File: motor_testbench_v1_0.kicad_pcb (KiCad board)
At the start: 4 copper layers, 130.5 x 74 mm, 156 parts, among them J1 Conn_01x03_Pin, J10 Conn_01x02_Pin, J11 Conn_01x02_Pin, J2 Conn_01x18_Pin, J3 V_bat_in, J4 V_bat_out, J5 Conn_01x05_Pin, J6 Conn_01x05_Pin, J7 Conn_01x05_Pin, J8 Conn_01x02_Pin, J9 V_bat_secondary, U1 ESP32-S3-DevKitC, U10 TPS7A20xxxDQN, U11 MCP1501-18xSN, U3 MCP6022, U4 ACPL-C87A, U5 TPS62933, U6 TLV77333PDBVR, U7 TPS62933, U8 TLV77333PDBVR, U9 TPS7A20xxxDQN

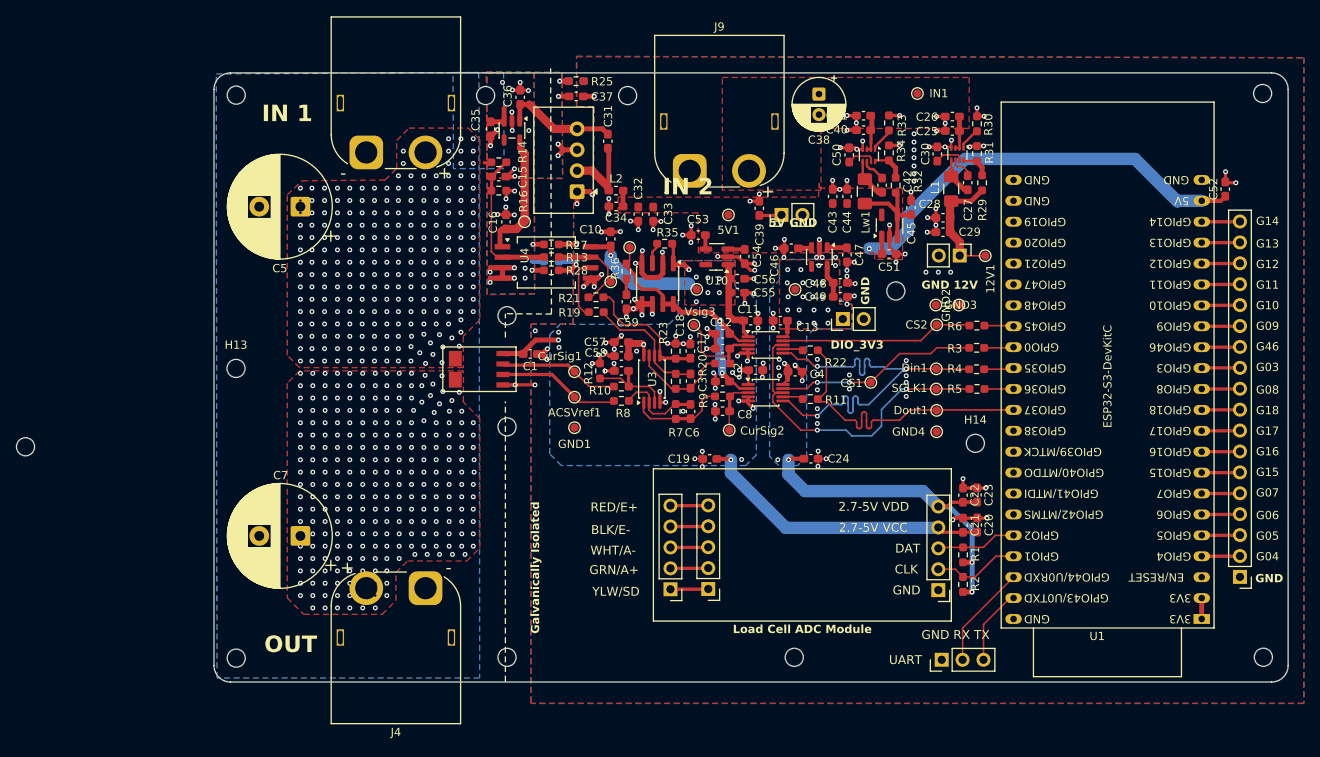
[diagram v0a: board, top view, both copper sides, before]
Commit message: Improved layout, added TVS diodes. Rotated ESP32, Changed proper SPI pins, finalized the load cell module area.
[KiCad Version: 9.0.8]
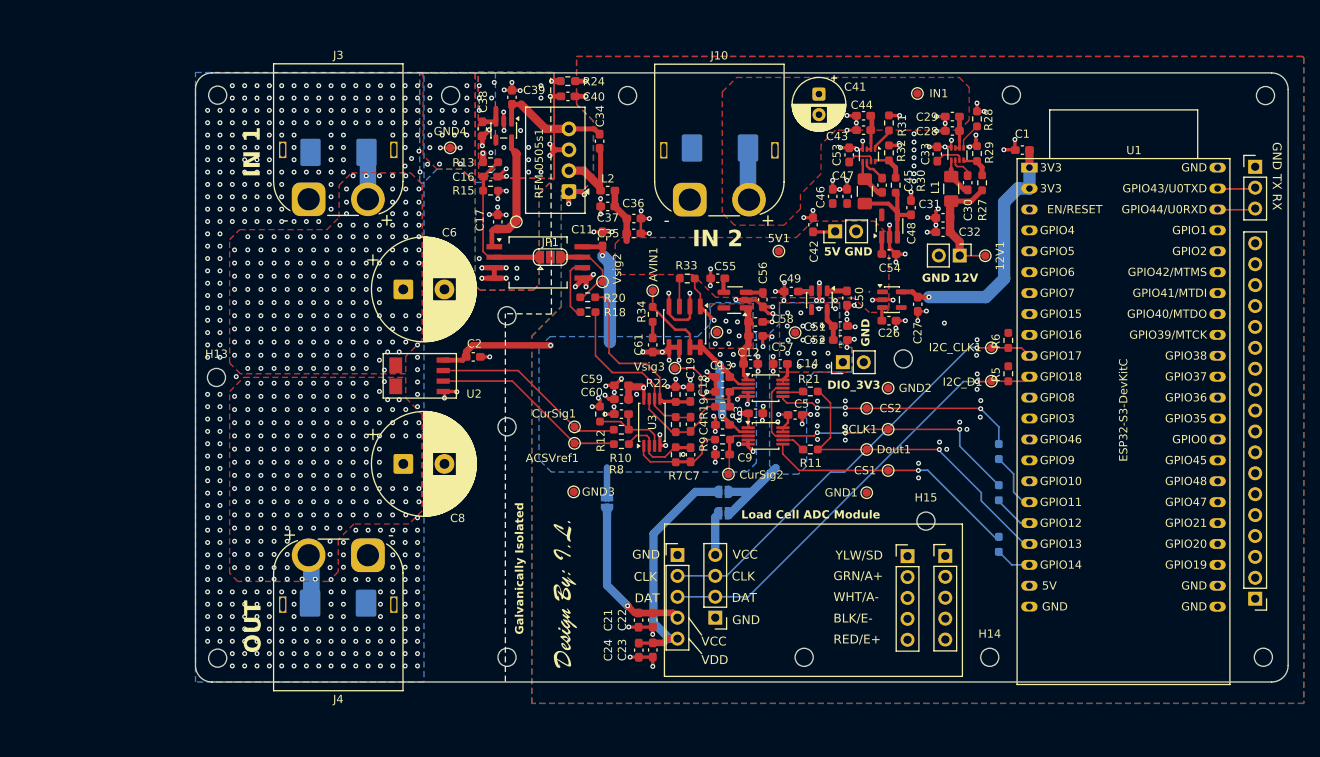
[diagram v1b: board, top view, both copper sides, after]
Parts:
- removed the C19 at (133.7, 86.4)
- removed the C24 at (146.0, 86.4)
- removed the C52 at (196.4, 53.6)
- removed Din1: TestPoint, TestPoint:TestPoint_Pad_D1.0mm
- removed the R13 at (114.5, 61.9)
- removed R26: 0R, Resistor_SMD:R_0603_1608Metric_Pad0.98x0.95mm_HandSolder
- removed the R27 at (114.5, 60.3)
- removed the R28 at (114.5, 63.5)
- removed the R4 at (166.2, 75.5)
- added C1: 1u, Capacitor_SMD:C_0603_1608Metric_Pad1.08x0.95mm_HandSolder, F.Cu at (171.7, 48.9)
- added C26: 1u, Capacitor_SMD:C_0603_1608Metric_Pad1.08x0.95mm_HandSolder, F.Cu at (155.5, 69.6)
- added C27: 2.2u, Capacitor_SMD:C_0603_1608Metric_Pad1.08x0.95mm_HandSolder, F.Cu at (159.0, 67.6)
- added D1: 1.5SMCxxCA, Diode_SMD:D_SMC, B.Cu at (88.6, 49.1)
- added D2: 1.5SMCxxCA, Diode_SMD:D_SMC, B.Cu at (88.6, 103.9)
- added D3: 1.5SMCxxCA, Diode_SMD:D_SMC, B.Cu at (135.0, 48.6)
- added G***: LOGO, LOGO, F.Cu at (117.8, 100.5)
- added G***: LOGO, LOGO, B.Cu at (181.5, 111.3)
- added H15: MountingHole, MountingHole:MountingHole_2.2mm_M2_DIN965, F.Cu at (160.0, 94.0)
- added I2C_CLK1: TestPoint, TestPoint:TestPoint_Pad_D1.0mm, F.Cu at (167.9, 72.9)
- added I2C_D1: TestPoint, TestPoint:TestPoint_Pad_D1.0mm, F.Cu at (167.9, 77.0)
- added J8: Conn_01x04_Pin, Connector_PinHeader_2.54mm:PinHeader_1x04_P2.54mm_Vertical, F.Cu at (134.4, 105.7)
- added JP1: SolderJumper_3_Open, Jumper:SolderJumper-3_P1.3mm_Open_RoundedPad1.0x1.5mm, F.Cu at (114.3, 61.9)
- added JP2: SolderJumper_2_Open, Jumper:SolderJumper-2_P1.3mm_Open_RoundedPad1.0x1.5mm, B.Cu at (121.2, 91.7)
- added JP3: SolderJumper_2_Open, Jumper:SolderJumper-2_P1.3mm_Open_RoundedPad1.0x1.5mm, B.Cu at (135.4, 90.4)
- added JP4: SolderJumper_2_Open, Jumper:SolderJumper-2_P1.3mm_Open_RoundedPad1.0x1.5mm, B.Cu at (135.4, 93.0)
- added JP5: SolderJumper_3_Open, Jumper:SolderJumper-3_P1.3mm_Open_RoundedPad1.0x1.5mm, B.Cu at (114.3, 61.9)
- added U5: TLV77333PDBVR, Package_TO_SOT_SMD:SOT-23-5, F.Cu at (155.9, 67.0)
- J10: renamed from J9; footprint Connector_AMASS:AMASS_XT60PW-M_1x02_P7.20mm_Horizontal -> custom_footprints:AMASS_XT60PW-M_1x02_P7.20mm_Horizontal_with3DModel
- J3, J4: footprint Connector_AMASS:AMASS_XT60PW-M_1x02_P7.20mm_Horizontal -> custom_footprints:AMASS_XT60PW-M_1x02_P7.20mm_Horizontal_with3DModel
- R2: renamed from R6; moved to B.Cu
- R3: renamed from R5; moved to B.Cu
- R4: renamed from R3; moved to B.Cu
- RFM-0505s1: footprint Converter_DCDC:Converter_DCDC_TRACO_TBA1-xxxx_THT -> custom_footprints:Converter_DCDC_TRACO_TBA1-xxxx_THT_with_3DModel
- U1: footprint ESP_footprints:ESP32-S3-DevKitC -> custom_footprints:ESP32-S3-DevKitC_with_3DModel
- U2: footprint custom_footprints:SOIC-6 -> custom_footprints:ACS37030LLZATR-065B3
- moved H3 107.2 mm to (157.2, 74.2)
- moved H1 73.2 mm to (170.4, 42.2)
- moved J1 71.0 mm to (200.0, 50.9), turned to 0 degrees
- moved GND4 68.4 mm to (102.2, 48.6)
- moved U1 58.7 mm to (172.6, 51.0), turned to 0 degrees
- moved GND3 49.5 mm to (117.2, 90.4)
- moved H2 45.9 mm to (145.2, 110.5)
- moved C24 45.2 mm to (125.1, 109.6), turned to 90 degrees
- moved C21 42.7 mm to (125.1, 106.0), turned to 90 degrees
- moved C23 42.1 mm to (126.8, 109.6), turned to 90 degrees
- moved C22 39.4 mm to (126.8, 106.0), turned to 90 degrees
- moved GND1 36.4 mm to (152.8, 90.5)
- moved J6 33.6 mm to (162.3, 98.2), turned to 0 degrees
- moved J7 32.0 mm to (129.8, 98.1), turned to 0 degrees
- moved R6 30.2 mm to (170.0, 72.0), turned to -90 degrees
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- renumbered C9 to C10, C10 to C11, C11 to C12, C12 to C13, C13 to C14, C14 to C15, C15 to C16, C16 to C17, C17 to C18, C18 to C19, C1 to C2, C20 to C21, C21 to C22, C22 to C23, C23 to C24, C25 to C28, C26 to C29, C2 to C3, C27 to C30, C28 to C31, C29 to C32, C30 to C33, C31 to C34, C32 to C35, C33 to C36, C34 to C37, C35 to C38, C36 to C39, C3 to C4, C37 to C40, C38 to C41, C39 to C42, C40 to C43, C41 to C44, C42 to C45, C43 to C46, C44 to C47, C45 to C48, C46 to C49, C4 to C5, C47 to C50, C48 to C51, C49 to C52, C50 to C53, C51 to C54, C53 to C55, C54 to C56, C55 to C57, C56 to C58, C57 to C59, C5 to C6, C58 to C60, C59 to C61, C6 to C7, C7 to C8, C8 to C9, J10 to J11, J11 to J12, J8 to J9, R14 to R13, R16 to R15, R18 to R17, R19 to R18, R20 to R19, R21 to R20, R22 to R21, R23 to R22, R24 to R23, R25 to R24, R29 to R27, R30 to R28, R31 to R29, R32 to R30, R33 to R31, R34 to R32, R35 to R33, R36 to R34, R1 to R5, R2 to R6, U9 to U10, U10 to U11, U11 to U12, U5 to U6, U6 to U7, U7 to U8, U8 to U9
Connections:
- C21 pad 2: 3V3_ANA -> Net-(J7-Pin_4)
- C22 pad 2: 3V3_ANA -> Net-(J7-Pin_4)
- C23 pad 2: 3V3_DIO -> Net-(J7-Pin_5)
- C24 pad 2: 3V3_DIO -> Net-(J7-Pin_5)
- Dout1 pad 1: D_out -> MISO
- GND4 pad 1: GND -> GND_ISO
- J5 pad 1: Net-(J5-Pin_1) -> unconnected-(J5-Pin_1-Pad1)
- J5 pad 2: Net-(J5-Pin_2) -> unconnected-(J5-Pin_2-Pad2)
- J5 pad 3: Net-(J5-Pin_3) -> unconnected-(J5-Pin_3-Pad3)
- J5 pad 4: Net-(J5-Pin_4) -> unconnected-(J5-Pin_4-Pad4)
- J5 pad 5: Net-(J5-Pin_5) -> unconnected-(J5-Pin_5-Pad5)
- J6 pad 1: Net-(J5-Pin_1) -> unconnected-(J6-Pin_1-Pad1)
- J6 pad 2: Net-(J5-Pin_2) -> unconnected-(J6-Pin_2-Pad2)
- J6 pad 3: Net-(J5-Pin_3) -> unconnected-(J6-Pin_3-Pad3)
- J6 pad 4: Net-(J5-Pin_4) -> unconnected-(J6-Pin_4-Pad4)
- J6 pad 5: Net-(J5-Pin_5) -> unconnected-(J6-Pin_5-Pad5)
- J7 pad 4: 3V3_ANA -> Net-(J7-Pin_4)
- J7 pad 5: 3V3_DIO -> Net-(J7-Pin_5)
- MCP1 pad 6: D_in -> CS1
- MCP1 pad 9: CS1 -> 3V3_DIO
- MCP2 pad 6: D_in -> CS2
- MCP2 pad 9: CS2 -> 3V3_DIO
- R11 pad 2: D_out -> MISO
- R2 pad 1: Net-(U1-GPIO45) -> Net-(U1-GPIO11/ADC2_CH0)
- R21 pad 2: D_out -> MISO
- R3 pad 1: Net-(U1-GPIO36) -> Net-(U1-GPIO12/ADC2_CH1)
- R4 pad 1: Net-(U1-GPIO0) -> Net-(U1-GPIO14/ADC2_CH3)
- R5 pad 1: 3V3_DIO -> ESP_3V3
- R6 pad 1: 3V3_DIO -> ESP_3V3
- U1 pad 1: Net-(U1-3V3-Pad1) -> ESP_3V3
- U1 pad 10: /10 -> I2C_CLK
- U1 pad 11: /11 -> I2C_D
- U1 pad 12: /12 -> unconnected-(U1-GPIO8/ADC1_CH7-Pad12)
- U1 pad 13: /13 -> unconnected-(U1-GPIO3/ADC1_CH2-Pad13)
- U1 pad 14: /46 -> unconnected-(U1-GPIO46-Pad14)
- U1 pad 15: /15 -> unconnected-(U1-GPIO9/ADC1_CH8-Pad15)
- U1 pad 16: /16 -> unconnected-(U1-GPIO10/ADC1_CH9-Pad16)
- U1 pad 17: /17 -> Net-(U1-GPIO11/ADC2_CH0)
- U1 pad 18: /18 -> Net-(U1-GPIO12/ADC2_CH1)
- U1 pad 19: /19 -> MISO
- U1 pad 2: Net-(U1-3V3-Pad1) -> ESP_3V3
- U1 pad 20: /20 -> Net-(U1-GPIO14/ADC2_CH3)
- U1 pad 21: 5V_bus -> unconnected-(U1-5V-Pad21)
- U1 pad 30: Net-(U1-GPIO45) -> unconnected-(U1-GPIO45-Pad30)
- U1 pad 31: Net-(U1-GPIO0) -> unconnected-(U1-GPIO0-Pad31)
- U1 pad 32: Net-(U1-GPIO35) -> unconnected-(U1-GPIO35-Pad32)
- U1 pad 33: Net-(U1-GPIO36) -> unconnected-(U1-GPIO36-Pad33)
- U1 pad 34: D_out -> unconnected-(U1-GPIO37-Pad34)
- U1 pad 4: /4 -> unconnected-(U1-GPIO4/ADC1_CH3-Pad4)
- U1 pad 40: I2C_D -> unconnected-(U1-GPIO2/ADC1_CH1-Pad40)
- U1 pad 41: I2C_CLK -> unconnected-(U1-GPIO1/ADC1_CH0-Pad41)
- U1 pad 42: Net-(J1-Pin_2) -> Net-(J1-Pin_3)
- U1 pad 43: Net-(J1-Pin_3) -> Net-(J1-Pin_2)
- U1 pad 5: /5 -> unconnected-(U1-GPIO5/ADC1_CH4-Pad5)
- U1 pad 6: /6 -> unconnected-(U1-GPIO6/ADC1_CH5-Pad6)
- U1 pad 7: /7 -> unconnected-(U1-GPIO7/ADC1_CH6-Pad7)
- U1 pad 8: /8 -> unconnected-(U1-GPIO15/ADC2_CH4/32K_P-Pad8)
- U1 pad 9: /9 -> unconnected-(U1-GPIO16/ADC2_CH5/32K_N-Pad9)
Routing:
- net D_in: track 51.7 -> 0.00 mm, vias 3 -> 0
- net 5V_bus: track 65.4 -> 20.5 mm, vias 1 -> 0
- net I2C_D: track 9.59 -> 53.9 mm, vias 0 -> 1
- net I2C_CLK: track 10.6 -> 54.9 mm, vias 0 -> 1
- net MISO: track 0.00 -> 39.5 mm, vias 0 -> 1
- net D_out: track 37.5 -> 0.00 mm
- net ESP_3V3: track 0.00 -> 31.8 mm, vias 0 -> 1
- net 3V3_DIO: track 53.3 -> 22.0 mm, vias 23 -> 20
- net Net-(J7-Pin_5): track 0.00 -> 29.4 mm
- net 3V3_ANA: track 82.5 -> 56.8 mm, vias 12 -> 11
- net Net-(J7-Pin_4): track 0.00 -> 20.5 mm, vias 0 -> 1
- net /Measurements/V_bat_in: track 1.03 -> 17.6 mm, vias 238 -> 174
- net GND: track 171.3 -> 160.3 mm, vias 159 -> 156
- net /Measurements/ACS_VREF: track 15.0 -> 24.3 mm
- net /Measurements/cur_sig: track 14.6 -> 23.8 mm
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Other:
- board size 130.5 x 74 mm -> 132.8 x 74 mm
- board text added: "GND TX RX"
- board text added: "VCC"
- board text added: "VDD"
- board text removed: "2.7-5V VCC"
- board text removed: "2.7-5V VDD"
- board text removed: "G03"
- board text removed: "G04"
- board text removed: "G05"
- board text removed: "G06"
- board text removed: "G07"
- board text removed: "G08"
- board text removed: "G09"
- board text removed: "G10"
- board text removed: "G11"
- board text removed: "G12"
- board text removed: "G13"
- board text removed: "G14"
- board text removed: "G15"
- board text removed: "G16"
- board text removed: "G17"
- board text removed: "G18"
- board text removed: "G46"
- board text removed: "GND RX TX"
- board text removed: "UART"

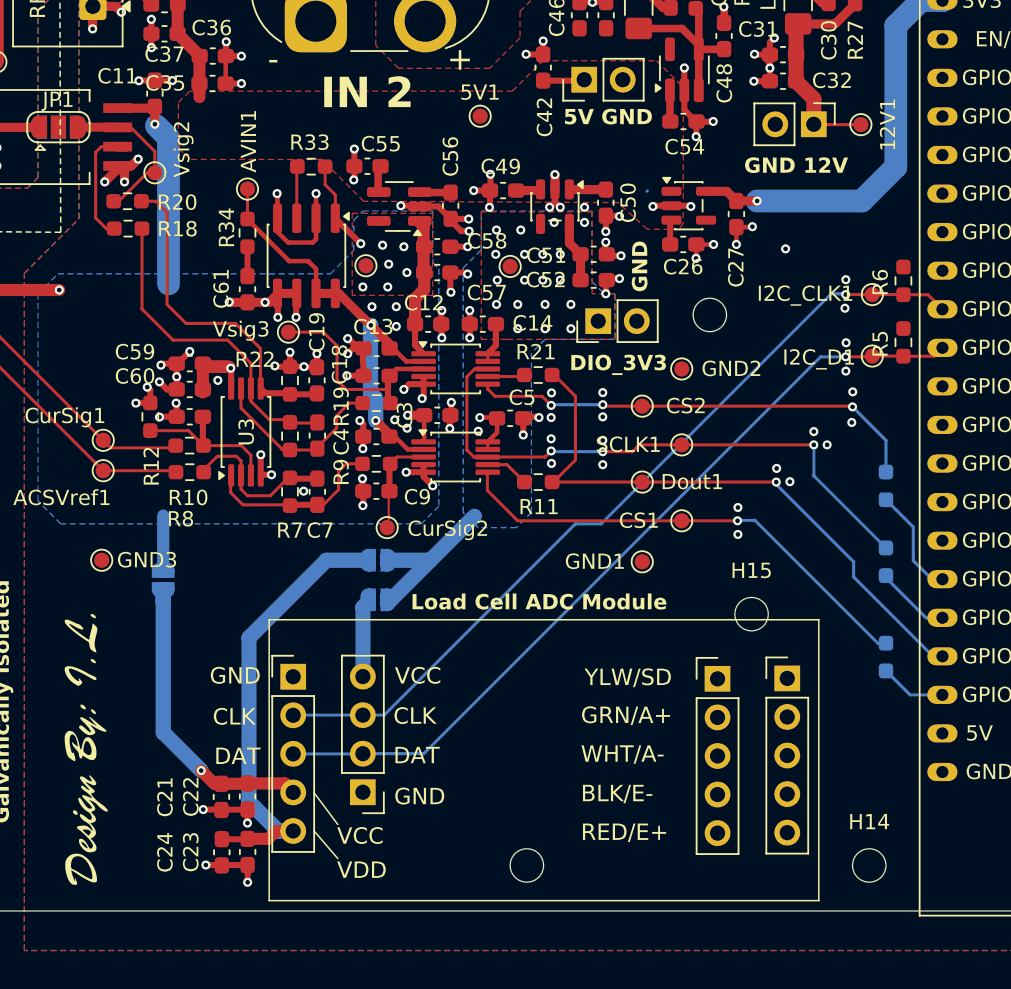
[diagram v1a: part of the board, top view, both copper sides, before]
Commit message: Moved the 1V8 Ref to bottom side of the board. Improved layout slightly / moved the Vref IC further away from hot / noisy side / further away from the noisy DCDC. Also managed to route the 1V8 and SPI more cleanly to the MCP ADCs.
[KiCad Version: 9.0.8]
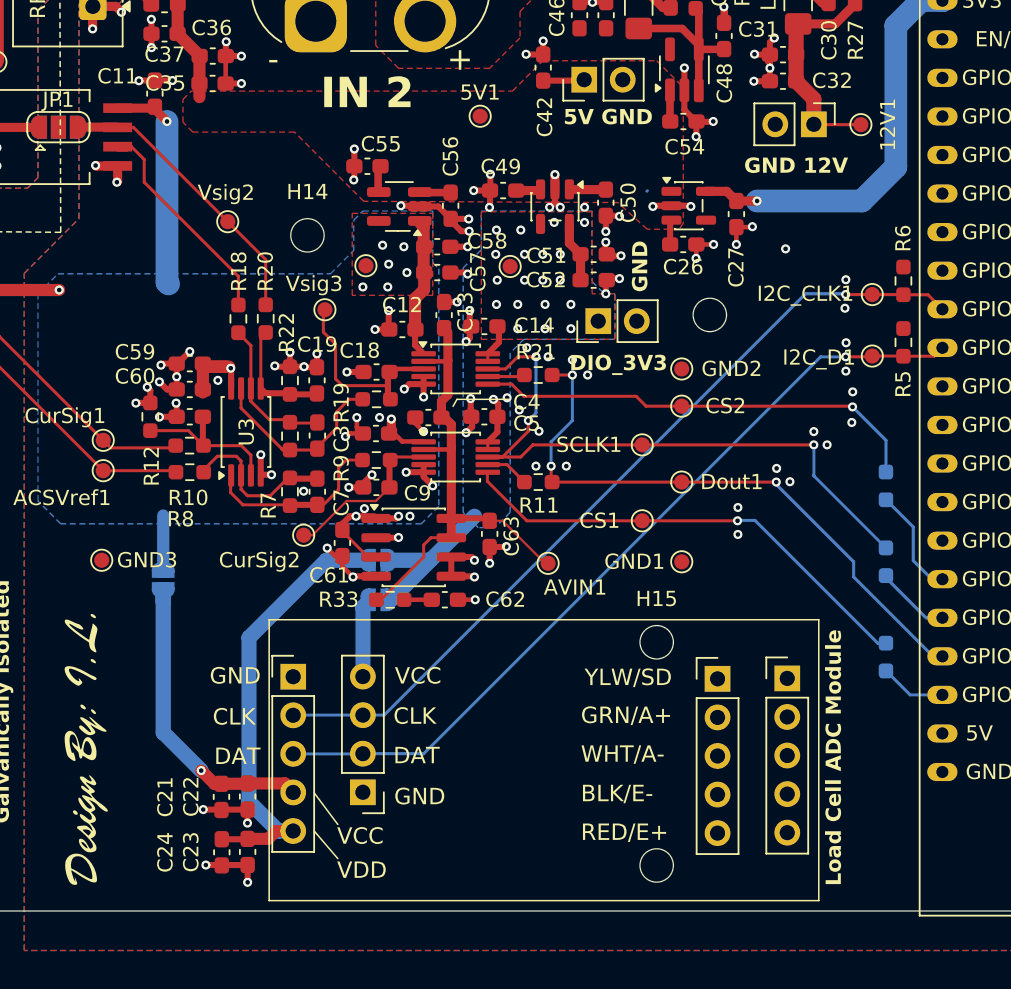
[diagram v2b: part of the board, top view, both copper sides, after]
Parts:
- removed the R33 at (131.0, 64.5)
- added C61: 2.2u, Capacitor_SMD:C_0603_1608Metric_Pad1.08x0.95mm_HandSolder, F.Cu at (133.1, 89.3)
- added C63: 2.2u, Capacitor_SMD:C_0603_1608Metric_Pad1.08x0.95mm_HandSolder, F.Cu at (142.8, 88.7)
- moved H14 55.6 mm to (130.8, 69.0)
- moved AVIN1 31.6 mm to (146.6, 90.6), turned to 90 degrees
- moved R33 25.9 mm to (136.2, 93.0), turned to 0 degrees
- moved C62 24.2 mm to (139.8, 93.0), turned to 180 degrees
- moved U12 20.5 mm to (137.8, 89.5), turned to 0 degrees
- moved R20 11.9 mm to (128.0, 74.5), turned to -90 degrees
- moved R18 9.39 mm to (126.2, 74.5), turned to -90 degrees
- moved H2 8.55 mm to (153.8, 110.5)
- moved H15 6.52 mm to (153.8, 95.8)
- moved Vsig2 5.78 mm to (125.5, 68.1)
- moved CurSig2 5.52 mm to (130.5, 88.8)
- moved C13 4.96 mm to (139.8, 74.2), turned to 90 degrees
- moved C3 4.21 mm to (135.3, 82.0), turned to 180 degrees
- moved C4 3.65 mm to (138.7, 81.0)
- moved Vsig3 2.82 mm to (131.9, 73.9)
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- renumbered C61 to C62, R34 to R33
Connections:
- U12 pad 3: Net-(U12-~{SHDN}) -> 3V3_ANA
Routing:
- net Net-(U3B-+): track 21.8 -> 7.63 mm
- net Net-(U3B--): track 21.2 -> 9.58 mm
- net GND: track 160.3 -> 152.0 mm, vias 156 -> 152
- net /Measurements/V_sig: track 10.8 -> 18.9 mm
- net /Measurements/Vout_ref: track 7.85 -> 14.9 mm
- net SCLK: track 38.6 -> 42.8 mm
- net Net-(MCP1-AIN+): track 6.71 -> 10.7 mm
- net 1V8_MCP_AVIN: track 28.9 -> 32.5 mm, vias 2 -> 0
- net Net-(U12-~{SHDN}): track 3.58 -> 0.00 mm
- net 3V3_ANA: track 56.8 -> 58.6 mm, vias 11 -> 12
- net Net-(MCP2-AIN+): track 13.7 -> 12.2 mm
- net MISO: track 39.5 -> 40.1 mm, vias 1 -> 3
- net CS2: track 30.1 -> 29.8 mm, vias 3 -> 1

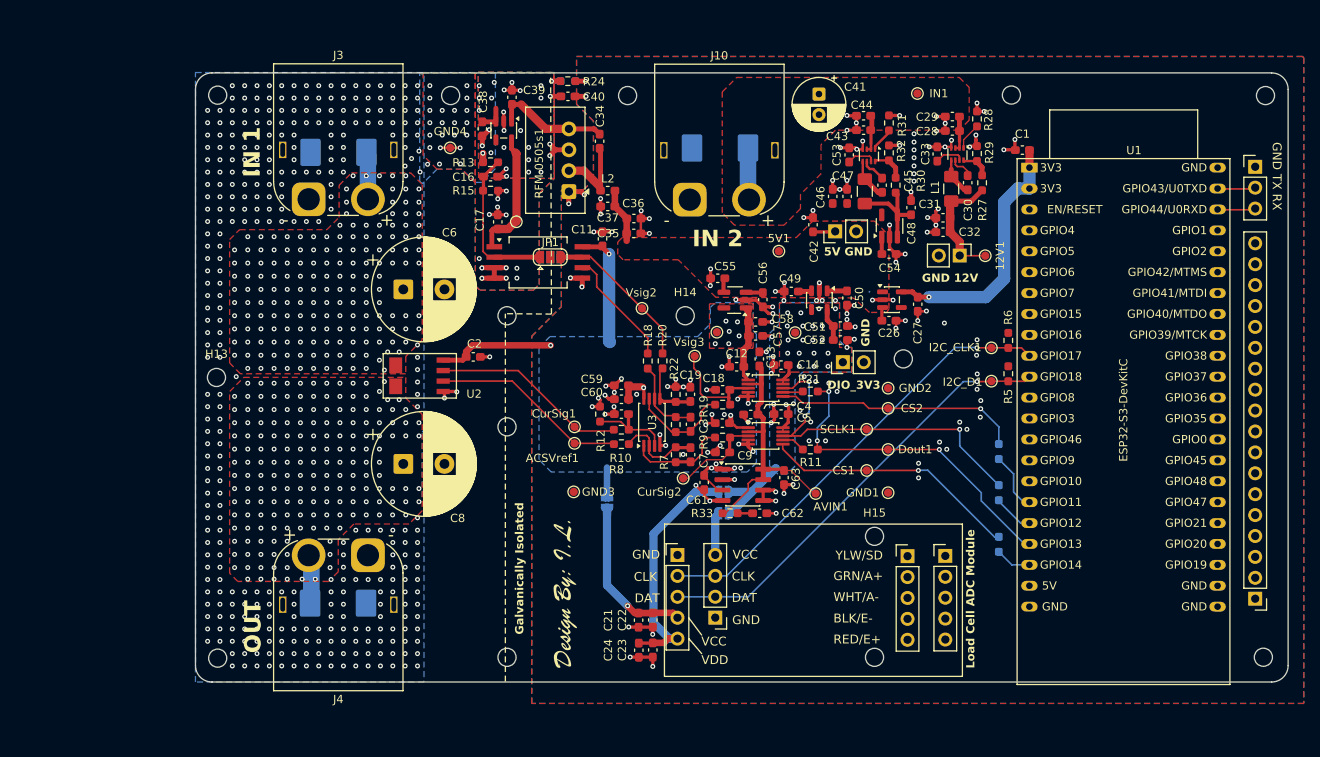
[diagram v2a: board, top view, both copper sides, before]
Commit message: Shortened high current path / improved the high current side layout.
[KiCad Version: 9.0.8]
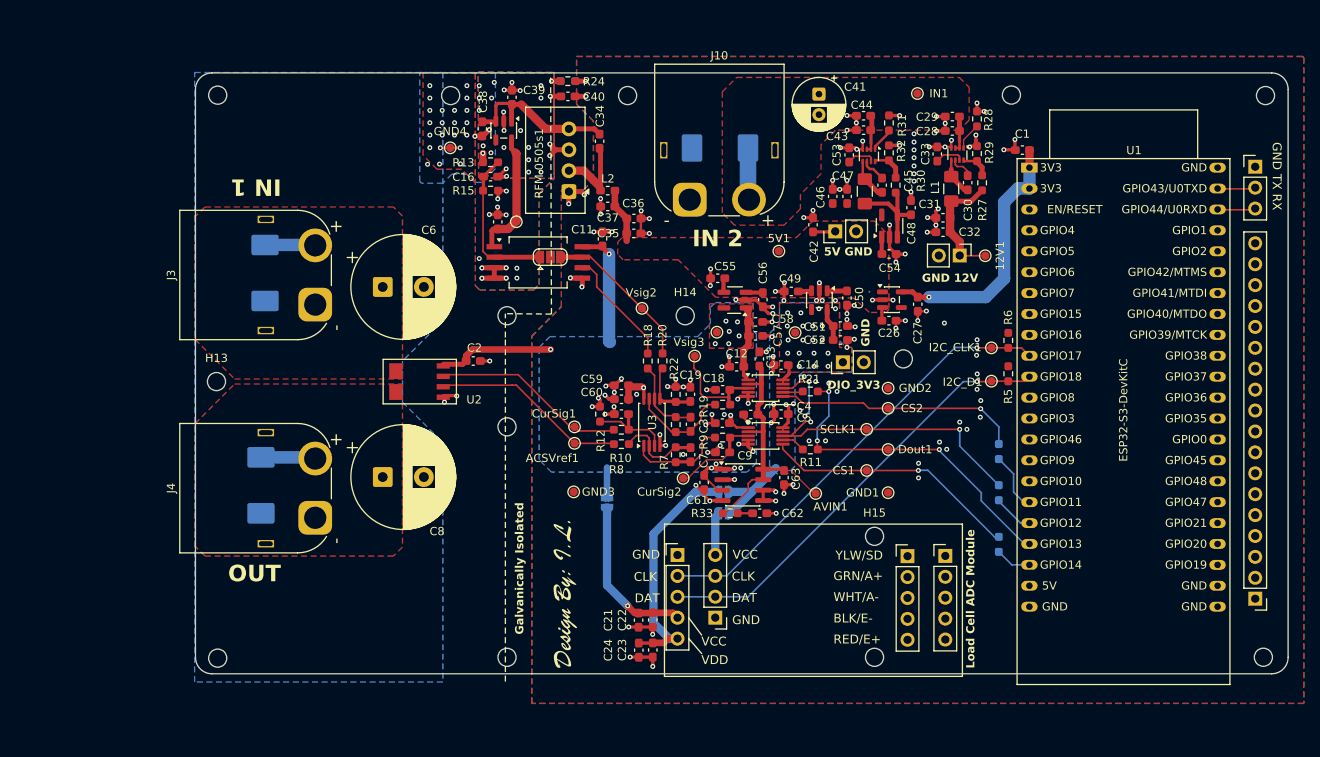
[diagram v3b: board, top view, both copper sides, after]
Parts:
- moved D1 17.2 mm to (79.7, 63.8), turned to 90 degrees
- moved D2 17.1 mm to (79.2, 89.6), turned to 90 degrees
- moved J3 12.8 mm to (85.8, 67.7), turned to 90 degrees
- moved J4 7.85 mm to (85.8, 93.5), turned to 90 degrees
- moved C8 2.97 mm to (94.0, 88.6)
- moved C6 2.52 mm to (94.0, 65.5)
- moved U2 0.70 mm to (98.8, 77.0)
- moved C2 0.50 mm to (105.0, 74.5)
- moved H13 0.50 mm to (73.8, 77.0)
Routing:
- net Net-(RFM-0505s1-Out+): track 17.5 -> 19.9 mm
- net /Measurements/V_bat_out: track 6.02 -> 6.66 mm, vias 182 -> 0
- net /Measurements/V_bat_in: track 17.6 -> 18.0 mm, vias 174 -> 1
- net GND_ISO: track 33.4 -> 33.1 mm, vias 421 -> 62
- removed copper zone on F.Cu, net /Measurements/V_bat_in
- removed copper zone on In1.Cu, net /Measurements/V_bat_in
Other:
- board size 132.8 x 74 mm -> 132.8 x 73 mm
